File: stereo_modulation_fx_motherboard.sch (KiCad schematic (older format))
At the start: 58 parts, among them J1 dry_out_A, J2 CV_out_A, J3 wet_in_A, J4 rez_CV_out_A, J5 dry_out_B, J6 CV_out_B, J7 wet_in_B, J8 rez_CV_out_B, SW1 sweep_mode, SW2 invert_B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

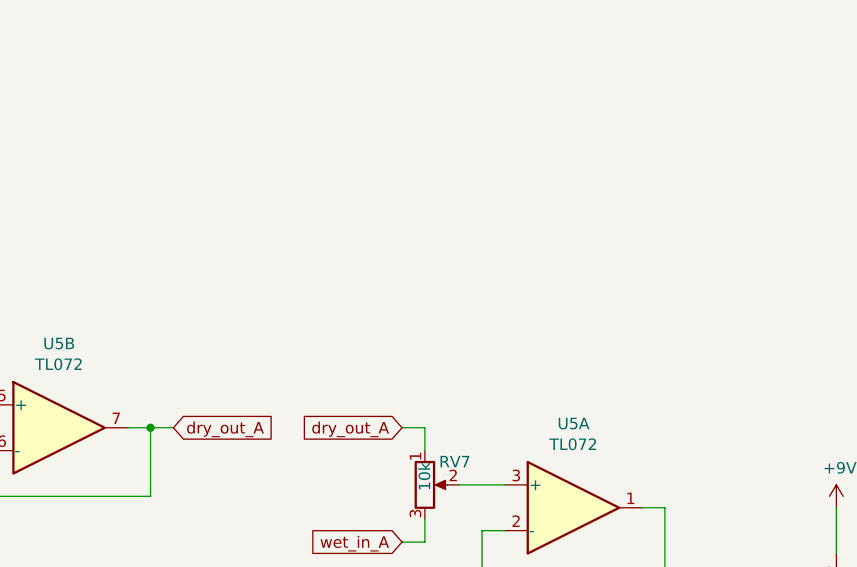
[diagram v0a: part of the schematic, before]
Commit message: add note about wet/dry mix polarity to schem, will need to be addressed
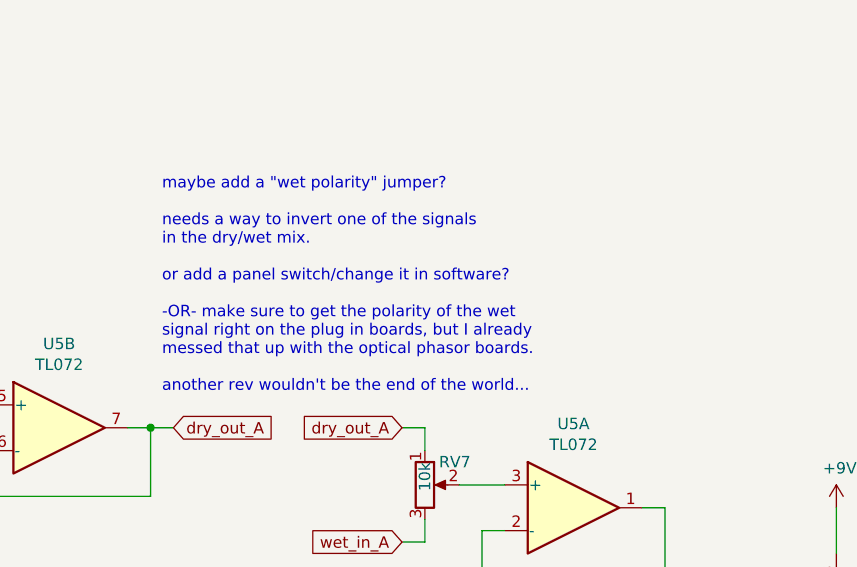
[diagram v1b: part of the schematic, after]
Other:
- note added: "maybe add a "wet polarity" jumper?\n\nneeds a way to invert one of the signals\nin the dry/wet mix.\n\nor add a panel switch/change it in software?\n\n-OR- make sure to get the polarity of the wet \nsignal right on the plug in boards, but I already \nmessed that up with the optical phasor boards.\n\nanother rev wouldn't be the end of the world..."
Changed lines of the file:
@@
 Wire Wire Line
 	15150 2650 15700 2650
+Text Notes 2950 13300 0    50   ~ 0
+maybe add a "wet polarity" jumper?\n\nneeds a way to invert one of the signals\nin the dry/wet mix.\n\nor add a panel switch/change it in software?\n\n-OR- make sure to get the polarity of the wet \nsignal right on the plug in boards, but I already \nmessed that up with the optical phasor boards.\n\nanother rev wouldn't be the end of the world...
 $EndSCHEMATC

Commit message: add wet/dry mix inverter, tidy up board, NOT DONE DO NOT ORDER BOARDS!
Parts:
- added JP1: mix polarity A, Connector_PinHeader_1.27mm:PinHeader_1x03_P1.27mm_Vertical_SMD_Pin1Left, symbol Device:Jumper_NC_Dual
- added JP2: mix polarity B, Connector_PinHeader_1.27mm:PinHeader_1x03_P1.27mm_Vertical_SMD_Pin1Left, symbol Device:Jumper_NC_Dual
- added R1, R2, R3, R4: 10k, Resistor_SMD:R_0805_2012Metric_Pad1.15x1.40mm_HandSolder, symbol Device:R
- gave numbers to parts that had none: 10
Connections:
- wire segments 304 -> 322
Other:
- note removed: "maybe add a "wet polarity" jumper?\n\nneeds a way to invert one of the signals\nin the dry/wet mix.\n\nor add a panel switch/change it in software?\n\n-OR- make sure to get the polarity of the wet \nsignal right on the plug in boards, but I already \nmessed that up with the optical phasor boards.\n\nanother rev wouldn't be the end of the world..."
- moved on the sheet: RV7, RV8, U5A, U5B, U5C, U6A, U6B, U6C

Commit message: add input buffers, misc tidy up, NOT DONE DO NOT ORDER BOARDS!
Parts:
- added C26, C27: 47nF, Capacitor_SMD:C_0805_2012Metric_Pad1.15x1.40mm_HandSolder, symbol Device:C
- added J10: Conn_01x04_Male, Connector_PinHeader_2.54mm:PinHeader_1x04_P2.54mm_Vertical, symbol Connector:Conn_01x04_Male
- added J11, J12: Conn_01x02_Male, Connector_PinHeader_2.54mm:PinHeader_1x02_P2.54mm_Vertical, symbol Connector:Conn_01x02_Male
- added R5, R6: 1M, Resistor_SMD:R_0805_2012Metric_Pad1.15x1.40mm_HandSolder, symbol Device:R
- added R7, R8: 220, Resistor_SMD:R_0805_2012Metric_Pad1.15x1.40mm_HandSolder, symbol Device:R
- added U7: TL072, Package_SO:SOIC-8_3.9x4.9mm_P1.27mm, symbol Amplifier_Operational:TL072
- renumbered U7 to U9
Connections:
- net labels added: input_A, input_B, output_A, output_B
- wire segments 322 -> 353
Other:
- note added: "TODO:\n\n-evaluate power supply\n\n-handle bypass switching (just do true bypass off-board?)\n\n-evaluate MUX/DEMUX\n\n-evaluate DACs\n\n-add ps bypass caps"
- moved on the sheet: R1, R2, R3, R4, RV7, RV8, U5A, U5B, U5C, U6A, U6B, U6C

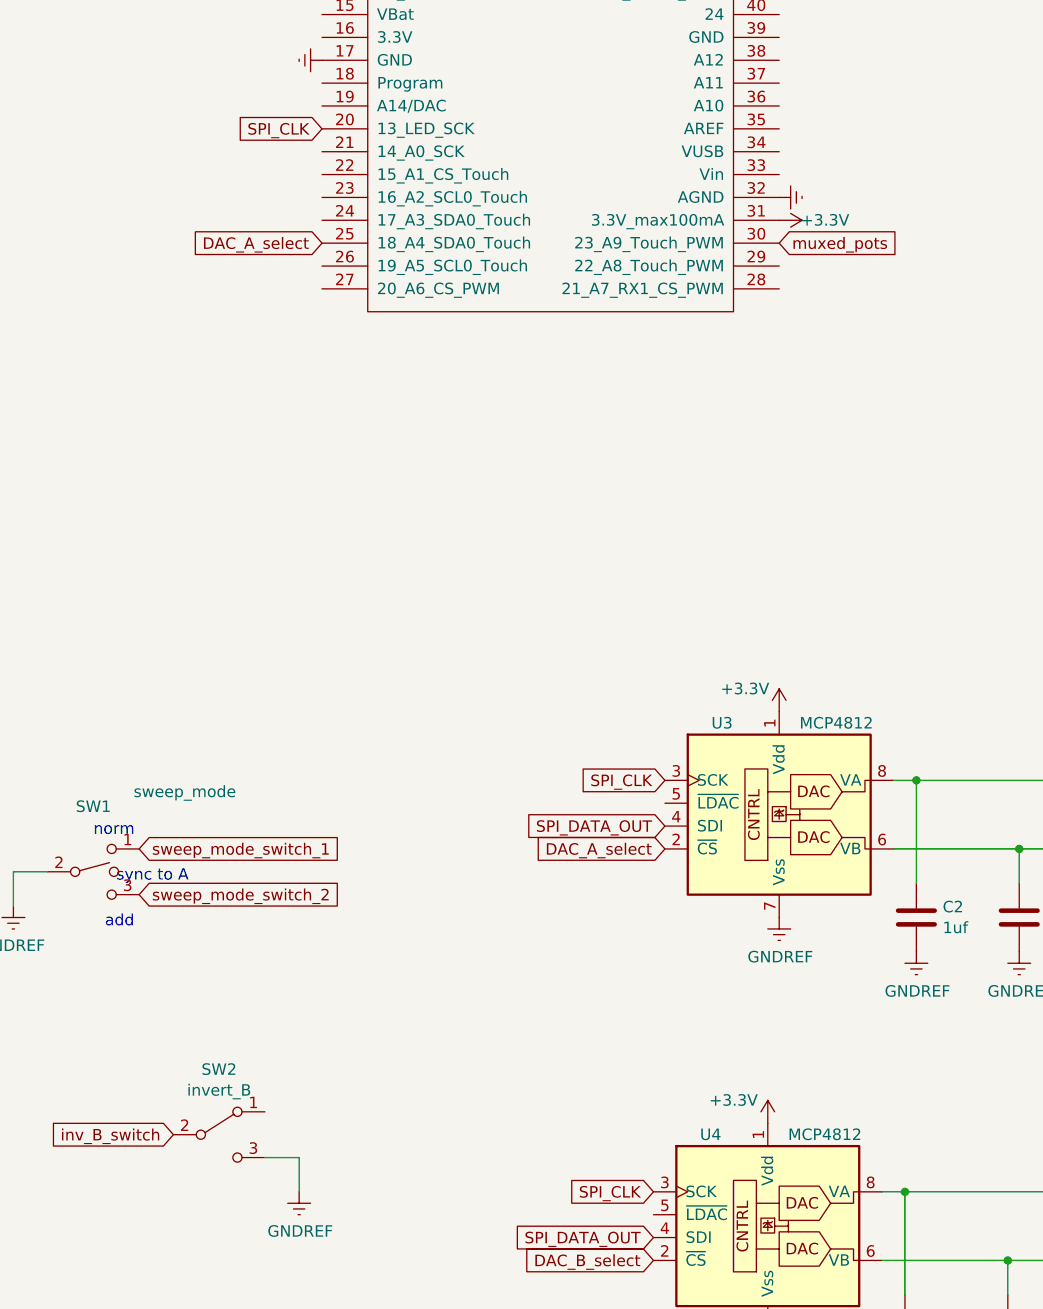
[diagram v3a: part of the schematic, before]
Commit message: change DACs to MCP4822, misc tidy up, DO NOT ORDER BOARDS!
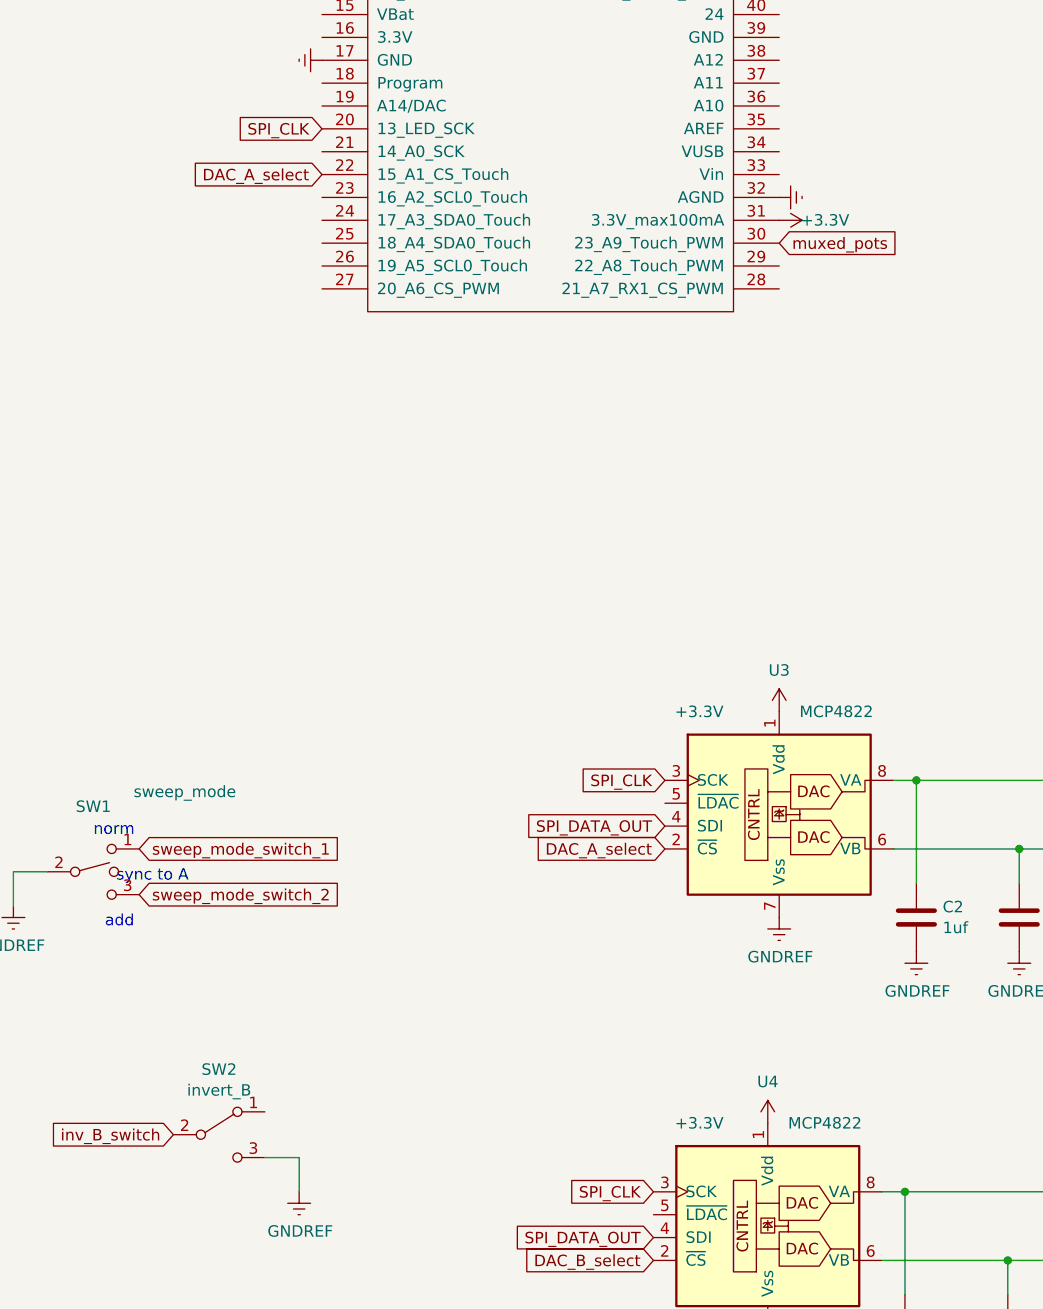
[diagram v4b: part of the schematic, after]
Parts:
- removed U3, U4: MCP4812, Package_SO:SOIC-8_3.9x4.9mm_P1.27mm, symbol Analog_DAC:MCP4812
- added U3, U4: MCP4822, Package_SO:SOIC-8_3.9x4.9mm_P1.27mm, symbol Analog_DAC:MCP4822
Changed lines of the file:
@@
 sweep_mode_switch_2
-$Comp
-L Analog_DAC:MCP4812 U3
-U 1 1 5CF10645
-P 9950 5850
-F 0 "U3" H 9700 6200 50  0000 C CNN
-F 1 "MCP4812" H 10200 6200 50  0000 C CNN
-F 2 "Package_SO:SOIC-8_3.9x4.9mm_P1.27mm" H 10750 5550 50  0001 C CNN
-F 3 "http://ww1.microchip.com/downloads/en/DeviceDoc/20002249B.pdf" H 10750 5550 50  0001 C CNN
-	1    9950 5850
-	1    0    0    -1
-$EndComp
 $Comp
 L power:GNDREF #PWR0105
@@
 $EndComp
 $Comp
-L Analog_DAC:MCP4812 U4
-U 1 1 5CF566EA
-P 9900 7650
-F 0 "U4" H 9650 8000 50  0000 C CNN
-F 1 "MCP4812" H 10150 8000 50  0000 C CNN
-F 2 "Package_SO:SOIC-8_3.9x4.9mm_P1.27mm" H 10700 7350 50  0001 C CNN
-F 3 "http://ww1.microchip.com/downloads/en/DeviceDoc/20002249B.pdf" H 10700 7350 50  0001 C CNN
-	1    9900 7650
-	1    0    0    -1
-$EndComp
-$Comp
 L power:+3.3V #PWR0106
 U 1 1 5CF566F4
 P 9900 7250
 F 0 "#PWR0106" H 9900 7100 50  0001 C CNN
-F 1 "+3.3V" H 9750 7350 50  0000 C CNN
+F 1 "+3.3V" H 9600 7250 50  0000 C CNN
 F 2 "" H 9900 7250 50  0001 C CNN
 F 3 "" H 9900 7250 50  0001 C CNN
@@
 Text GLabel 9450 6050 0    50   Input ~ 0
 DAC_A_select
-Text GLabel 7950 3400 0    50   Input ~ 0
+Text GLabel 7950 3100 0    50   Input ~ 0
 DAC_A_select
 Text GLabel 9400 7850 0    50   Input ~ 0
@@
 P 9950 5450
 F 0 "#PWR0104" H 9950 5300 50  0001 C CNN
-F 1 "+3.3V" H 9800 5550 50  0000 C CNN
+F 1 "+3.3V" H 9600 5450 50  0000 C CNN
 F 2 "" H 9950 5450 50  0001 C CNN
 F 3 "" H 9950 5450 50  0001 C CNN
@@
 Wire Wire Line
 	16550 2650 16200 2650
+$Comp
+L Analog_DAC:MCP4822 U3
+U 1 1 5CF0D768
+P 9950 5850
+F 0 "U3" H 9950 6431 50  0000 C CNN
+F 1 "MCP4822" H 10200 6250 50  0000 C CNN
+F 2 "Package_SO:SOIC-8_3.9x4.9mm_P1.27mm" H 10750 5550 50  0001 C CNN
+F 3 "http://ww1.microchip.com/downloads/en/DeviceDoc/20002249B.pdf" H 10750 5550 50  0001 C CNN
+	1    9950 5850
+	1    0    0    -1
+$EndComp
+$Comp
+L Analog_DAC:MCP4822 U4
+U 1 1 5CF15BA5
+P 9900 7650
+F 0 "U4" H 9900 8231 50  0000 C CNN
+F 1 "MCP4822" H 10150 8050 50  0000 C CNN
+F 2 "Package_SO:SOIC-8_3.9x4.9mm_P1.27mm" H 10700 7350 50  0001 C CNN
+F 3 "http://ww1.microchip.com/downloads/en/DeviceDoc/20002249B.pdf" H 10700 7350 50  0001 C CNN
+	1    9900 7650
+	1    0    0    -1
+$EndComp
 $EndSCHEMATC

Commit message: remove wet/dry mixer, replace with envelope follower, NOT DONE DO NOT ORDER BOARDS!
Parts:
- removed J11, J12: Conn_01x02_Male, Connector_PinHeader_2.54mm:PinHeader_1x02_P2.54mm_Vertical, symbol Connector:Conn_01x02_Male
- removed JP1: mix polarity A, Connector_PinHeader_1.27mm:PinHeader_1x03_P1.27mm_Vertical_SMD_Pin1Left, symbol Device:Jumper_NC_Dual
- removed JP2: mix polarity B, Connector_PinHeader_1.27mm:PinHeader_1x03_P1.27mm_Vertical_SMD_Pin1Left, symbol Device:Jumper_NC_Dual
- removed R4: 10k, Resistor_SMD:R_0805_2012Metric_Pad1.15x1.40mm_HandSolder, symbol Device:R
- removed U6: TL072, Package_SO:SOIC-8_3.9x4.9mm_P1.27mm, symbol Amplifier_Operational:TL072
- added C28, C29, C39: 100nF, Capacitor_SMD:C_0805_2012Metric_Pad1.15x1.40mm_HandSolder, symbol Device:C
- added C30, C31: 470nF, Capacitor_SMD:C_0805_2012Metric_Pad1.15x1.40mm_HandSolder, symbol Device:C
- added C37, C38: 4.7nF, Capacitor_SMD:C_0805_2012Metric_Pad1.15x1.40mm_HandSolder, symbol Device:C
- added C? (x2): 4.7uF, symbol Device:CP1
- added D? (x4): D, symbol Device:D
- added J11, J12: Conn_01x04_Male, Connector_PinHeader_2.54mm:PinHeader_1x04_P2.54mm_Vertical, symbol Connector:Conn_01x04_Male
- added R13, R14: 120k, Resistor_SMD:R_0805_2012Metric_Pad1.15x1.40mm_HandSolder, symbol Device:R
- added R15, R16: 82k, Resistor_SMD:R_0805_2012Metric_Pad1.15x1.40mm_HandSolder, symbol Device:R
- added R17: 15k, Resistor_SMD:R_0805_2012Metric_Pad1.15x1.40mm_HandSolder, symbol Device:R
- added R18: 27k, Resistor_SMD:R_0805_2012Metric_Pad1.15x1.40mm_HandSolder, symbol Device:R
- added R19, R20, R9, R? (x2): ???, Resistor_SMD:R_0805_2012Metric_Pad1.15x1.40mm_HandSolder, symbol Device:R
- added R? (x2): 330, symbol Device:R
- added R? (x2): 47k, symbol Device:R
- added U6, U8: MCP6002-xSN, Package_SO:SOIC-8_3.9x4.9mm_P1.27mm, symbol Amplifier_Operational:MCP6002-xSN
- C26, C27: value 47nF -> 10nF
- R1, R2: value 10k -> 15k
- R3: value 10k -> ???
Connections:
- net labels added: CV_amp_bias, LFO_rate_CV_in, env_A, env_B, env_follower_A_in, env_follower_A_out, env_follower_B_in, env_follower_B_out, freq_CV_in, scaled_LFO_rate_CV, scaled_freq_CV
- wire segments 353 -> 445
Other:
- note added: "0V to +5V"
- note added: "12 bit DACs"
- note added: "3.3V to 0V"
- note added: "CV input scalers"
- note added: "LFO mode switches"
- note added: "TODO:\n\n-evaluate power supply\n\n-figure out how to do the envelope follower/digitize the audio?\n\n- figure out CV in circuit\n\n-handle bypass switching (just do true bypass off-board?)\n\n-evaluate MUX/DEMUX\n\n-evaluate DACs (DACs work, but output max of 2.048 volts...\nthis might be fine, just need to scale it up on plug in boards...\nsee mcp4822_test in platformio projects)\n\n-add ps byp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"
- note added: "between 2.12V and 2.16V is ideal.\nextra resistor pads R19 and R20 are for trimming if needed.\nthis isn't really all that critical."
- note added: "demux"
- note added: "envelope followers"
- note added: "input/output buffers"
- note added: "potentiometers"
- note removed: "TODO:\n\n-evaluate power supply\n\n-handle bypass switching (just do true bypass off-board?)\n\n-evaluate MUX/DEMUX\n\n-evaluate DACs\n\n-add ps bypass caps"
- moved on the sheet: C1, C13, C14, C15, C16, C17, C18, C19, C2, C20, C21, C22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

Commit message: continue working on layout, NOT DONE!
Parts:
- removed C5, C6, C7, C8, C9: 100nF, Capacitor_SMD:C_0805_2012Metric_Pad1.15x1.40mm_HandSolder, symbol Device:C
- removed C? (x2): 4.7uF, symbol Device:CP1
- removed D? (x4): D, symbol Device:D
- removed R? (x2): 330, symbol Device:R
- removed R? (x2): 47k, symbol Device:R
- added C32: 100nF, Capacitor_SMD:C_0805_2012Metric_Pad1.15x1.40mm_HandSolder, symbol Device:C
- added C33, C34, C35, C36: C, Capacitor_SMD:C_0805_2012Metric_Pad1.15x1.40mm_HandSolder, symbol Device:C
- added R11, R12: 10k, Resistor_SMD:R_0805_2012Metric_Pad1.15x1.40mm_HandSolder, symbol Device:R
- added SW3: DPDT_on_on_on, stereo_modulation_fx_motherboard_custom_footprints:DPDT_on_on_on, symbol stereo_modulation_fx_motherboard_custom_parts:DPDT_on_on_on
- SW1, SW2: footprint stereo_modulation_fx_motherboard_custom_footprints:NKK_M201xSS1W03 -> stereo_modulation_fx_motherboard_custom_footprints:SPDT_on_on
- gave numbers to parts that had none: 2
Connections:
- net env_follower_A_out is gone; now on net A_to_uC: U2.5 (I4)
- net env_follower_B_out is gone; now on net B_to_uC: U2.4 (I5)
- net +3V3: now also R11.1
- net env_A: now also U2.23 (I8); no longer U2.22 (I9)
- net input_A: now also C26.2; no longer C27.2
- net input_B: now also C27.2; no longer C26.2
- net inv_B_switch: now also SW2.1 (A); no longer SW2.2 (B)
- net output_A: now also R7.1; no longer R8.1
- net output_B: now also R8.1; no longer R7.1
- net rez_B: now also U2.22 (I9); no longer U2.23 (I8)
- net scaled_LFO_rate_CV: now also C37.1, R15.1, U6.1; no longer C38.1, R16.1, U6.7
- net scaled_freq_CV: now also C38.1, R16.1, U6.7; no longer C37.1, R15.1, U6.1
- net at C37.2, R15.2, U6.2 (-): now also R14.1; no longer R13.1
- net at C38.2, R16.2, U6.6 (-): now also R13.1; no longer R14.1
- net A_to_uC: now reaches R9.1
- net A_to_uC: now also U8.1, C36.1
- net at R3.1, R9.2, U8.2 (-): now also C36.2
- net at R10.2, R4.1, U8.6 (-): now also C35.2
- net B_to_uC: now reaches U8.7
- net B_to_uC: now also R10.1, C35.1
- net at R3.2: now also C34.1
- net at R4.2: now also C33.1
- net GNDREF renamed GNDA
- net GNDA: now also SW2.2 (B), C32.2, R12.2; no longer SW2.3 (C), U1.17 (GND), U8.3 (+), U8.5 (+)
- net dry_out_A: no longer names the net of U7.6 (-), U7.7
- net dry_out_A: now also SW3.6; no longer J1.3 (Pin_3), J1.4 (Pin_4)
- net dry_out_B renamed dry_A
- net dry_A: now also J1.3 (Pin_3), J1.4 (Pin_4), C34.2, SW3.1; no longer J5.3 (Pin_3), J5.4 (Pin_4)
- net wet_in_A renamed wet_A
- net wet_A: now also C30.2, SW3.4; no longer C31.2
- net wet_in_B renamed wet_B
- net wet_B: now also C31.2; no longer C30.2
- new net audio_to_uC_amp_bias: C32.1, R11.2, R12.1, U8.3 (+), U8.5 (+)
- new net dry_B: C33.2, J5.3 (Pin_3), J5.4 (Pin_4), SW3.2
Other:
- note added: "TODO:\n\n-evaluate power supply\n\n-triple check all footprints!!!\n\n-figure out how to do the envelope follower/digitize the audio?\n\n- figure out CV in circuit\n\n-handle bypass switching (just do true bypass off-board?)\n\n-evaluate MUX/DEMUX\n\n-evaluate DACs (DACs work, but output max of 2.048 volts...\nthis might be fine, just need to scale it up on plug in boards...\nsee mcp4822_test in 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"
- note added: "audio to uC amplifiers"
- note removed: "TODO:\n\n-evaluate power supply\n\n-figure out how to do the envelope follower/digitize the audio?\n\n- figure out CV in circuit\n\n-handle bypass switching (just do true bypass off-board?)\n\n-evaluate MUX/DEMUX\n\n-evaluate DACs (DACs work, but output max of 2.048 volts...\nthis might be fine, just need to scale it up on plug in boards...\nsee mcp4822_test in platformio projects)\n\n-add ps byp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"
- note removed: "envelope followers"
- moved on the sheet: C26, C27, C30, C31, C37, C38, C39, J10, J12, R1, R10, R13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

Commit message: move all components to one side of board, play with trace layout, NOT DONEgit add -A!
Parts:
- added J13, J14: Conn_01x02_Male, Connector_PinHeader_2.54mm:PinHeader_1x02_P2.54mm_Vertical, symbol Connector:Conn_01x02_Male
- added U10, U11: DG419LDY, Package_SO:SOIC-8_3.9x4.9mm_P1.27mm, symbol Analog_Switch:DG419LDY
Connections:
- net +3V3: now also U10.5 (VL), U11.5 (VL)
- net A_to_uC: now also U2.20 (I11); no longer U2.5 (I4)
- net B_to_uC: now also U2.21 (I10); no longer U2.4 (I5)
- net GNDA: now also J13.2 (Pin_2), J14.2 (Pin_2), U10.3 (GND), U11.3 (GND)
- net depth_A: now also U2.8 (I1); no longer U2.18 (I13)
- net depth_B: now also U2.18 (I13); no longer U2.7 (I2)
- net dry_A: now also U10.2
- net env_A: now also U2.6 (I3); no longer U2.23 (I8)
- net env_B: now also U2.3 (I6); no longer U2.20 (I11)
- net manual_freq: now also U2.17 (I14); no longer U2.9 (I0)
- net mux_S0: now also U1.27 (20_A6_CS_PWM); no longer U1.6 (4_RX_PWM)
- net mux_S1: now also U1.26 (19_A5_SCL0_Touch); no longer U1.7 (5_TX1_PWM)
- net mux_S2: now also U1.29 (22_A8_Touch_PWM); no longer U1.5 (3_TX_PWM)
- net mux_S3: now also U1.30 (23_A9_Touch_PWM); no longer U1.4 (2)
- net muxed_pots: now also U1.28 (21_A7_RX1_CS_PWM); no longer U1.30 (23_A9_Touch_PWM)
- net rate_A: now also U2.9 (I0); no longer U2.17 (I14)
- net rate_B: now also U2.19 (I12); no longer U2.6 (I3)
- net rez_A: now also U2.5 (I4); no longer U2.21 (I10)
- net rez_B: now also U2.4 (I5); no longer U2.22 (I9)
- net scaled_LFO_rate_CV: now also U2.23 (I8); no longer U2.3 (I6)
- net scaled_freq_CV: now also U2.22 (I9); no longer U2.2 (I7)
- net shape_A: now also U2.7 (I2); no longer U2.19 (I12)
- net shape_B: now also U2.2 (I7); no longer U2.8 (I1)
- net wet_A: now also U10.8; no longer C30.2
- net wet_B: now also U11.8; no longer C31.2
- net at SW3.6, U7.6 (-), U7.7: now also U11.2
- net bypass_B: now reaches U1.24 (17_A3_SDA0_Touch)
- net bypass_B: now also U11.6
- net bypass_A: now reaches U1.25 (18_A4_SDA0_Touch)
- net bypass_A: now also U10.6
- net +9V renamed +12V
- net +12V: now also U10.4 (V+), U11.4 (V+)
- net -9V renamed -12V
- net -12V: now also U10.7 (V-), U11.7 (V-)
- new net: C30.2, U10.1
- new net: C31.2, U11.1
- new net footswitch_A: J13.1 (Pin_1), U1.6 (4_RX_PWM)
- new net footswitch_B: J14.1 (Pin_1), U1.7 (5_TX1_PWM)
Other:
- note added: "footswitches"
- moved on the sheet: C26, C27, C30, C31, J10, J11, R1, R2, R5, R6, R7, R8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
